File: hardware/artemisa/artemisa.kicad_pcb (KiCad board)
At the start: 2 copper layers, 140 parts, among them J1 PS2_CONN, J2 MSX_Slot, J3 MSX_Slot, J4 CONN_JOY, J5 CONN_JOY, J6 PWR_conn, J7 Audio_conn, J8 Audio_conn, J9 GFX_Connector_Output, U1 74HC32, U11 74HCT244, U12 74HCT244, U13 74HCT245, U14 74HCT244, U15 74HC74, U16 74HC08, U17 74HC32, U18 Z84C00, U19 82C55A, U2 74HC04, U20 74HC153, U21 74HC139, U22 LM311, U23 74HC138, U24 74HC32, U25 SST39SF0x0, U26 ATMEGA328P, U27 74HC154, U28 74HC595, U29 74HC595, U3 HM62256ALP-10, U30 74HC595, U31 74HC595, U32 74HC595, U33 74HC595, U34 74HC595, U35 74HC595, U36 74HC595, U37 74HC595, U38 4069, U39 74HC07, U4 HM62256ALP-10, U40 74HC74, U41 AY-3-8910, U42 74HC157, U43 74HC157, U44 74HC595, U5 74HCT11, Y1 3.58Mhz, Y2 16Mhz

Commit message: Complete layout of footprints for 25x15cm
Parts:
- added G***: LOGO, artemisa:MSX_logo, F.Cu at (62.9, 92.7)
- moved U25 135.6 mm to (228.6, 124.5)
- moved DC25 129.9 mm to (237.5, 120.7)
- moved DC26 117.7 mm to (288.9, 207.6), turned to 270 degrees
- moved C3 105.5 mm to (284.5, 201.3), turned to 0 degrees
- moved R19 104.8 mm to (132.7, 190.5)
- moved U26 104.6 mm to (292.7, 192.4)
- moved Y2 102.1 mm to (280.0, 208.8)
- moved C4 102.0 mm to (284.5, 215.3), turned to 0 degrees
- moved U1 99.6 mm to (229.2, 179.7), turned to 90 degrees
- moved U33 93.5 mm to (282.6, 188.0), turned to 90 degrees
- moved U44 92.6 mm to (282.6, 124.5), turned to 90 degrees
- moved U17 92.1 mm to (77.5, 153.0)
- moved DC17 92.1 mm to (82.5, 149.2)
- moved DC1 90.7 mm to (225.4, 174.7), turned to 270 degrees
- moved DC44 90.2 mm to (278.8, 119.4), turned to 270 degrees
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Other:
- board text added: "Artemisa MSX Computer System Motherboard Rev01 Copyright (c) 2018 Alvaro Polo"

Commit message: Add decoupling capacitors for power input
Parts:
- added C14: 10uF, artemisa:Radial_capacitor, F.Cu at (74.3, 104.2)
- added C15: 100uF, artemisa:Radial_capacitor, F.Cu at (85.7, 104.2)

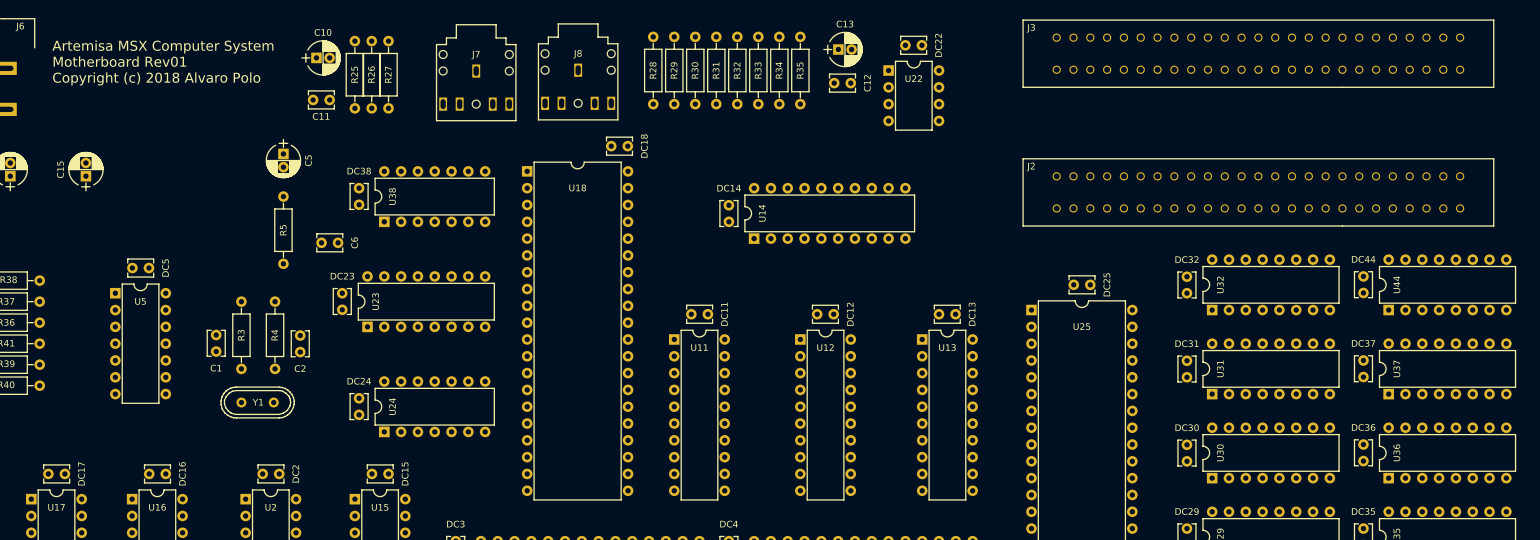
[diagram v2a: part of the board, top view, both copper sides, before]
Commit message: Make room for cartridge slots
We need more space according to cartridge specs.
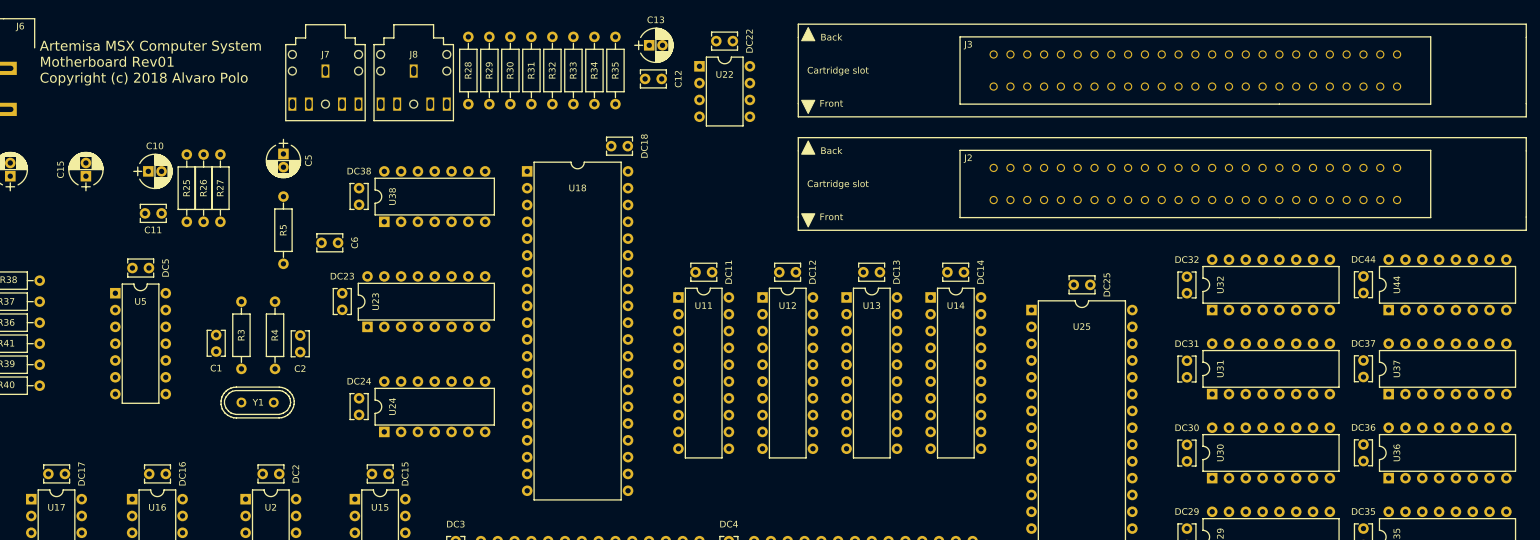
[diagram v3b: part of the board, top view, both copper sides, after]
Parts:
- moved DC14 36.9 mm to (218.4, 118.7), turned to 180 degrees
- moved C11 30.6 mm to (97.2, 109.9)
- moved R26 30.6 mm to (103.5, 101.0)
- moved C10 30.6 mm to (95.2, 103.5)
- moved R25 30.6 mm to (101.0, 111.1)
- moved R27 30.6 mm to (106.0, 111.1)
- moved DC22 28.6 mm to (183.5, 83.8)
- moved C12 28.6 mm to (172.7, 89.5)
- moved C13 28.6 mm to (170.8, 84.5)
- moved U22 28.6 mm to (178.4, 87.6)
- moved U14 28.1 mm to (213.4, 122.6), turned to 0 degrees
- moved R28 27.9 mm to (143.5, 93.3)
- moved R29 27.9 mm to (146.7, 93.3)
- moved R30 27.9 mm to (149.9, 83.2)
- moved R31 27.9 mm to (153.0, 93.3)
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
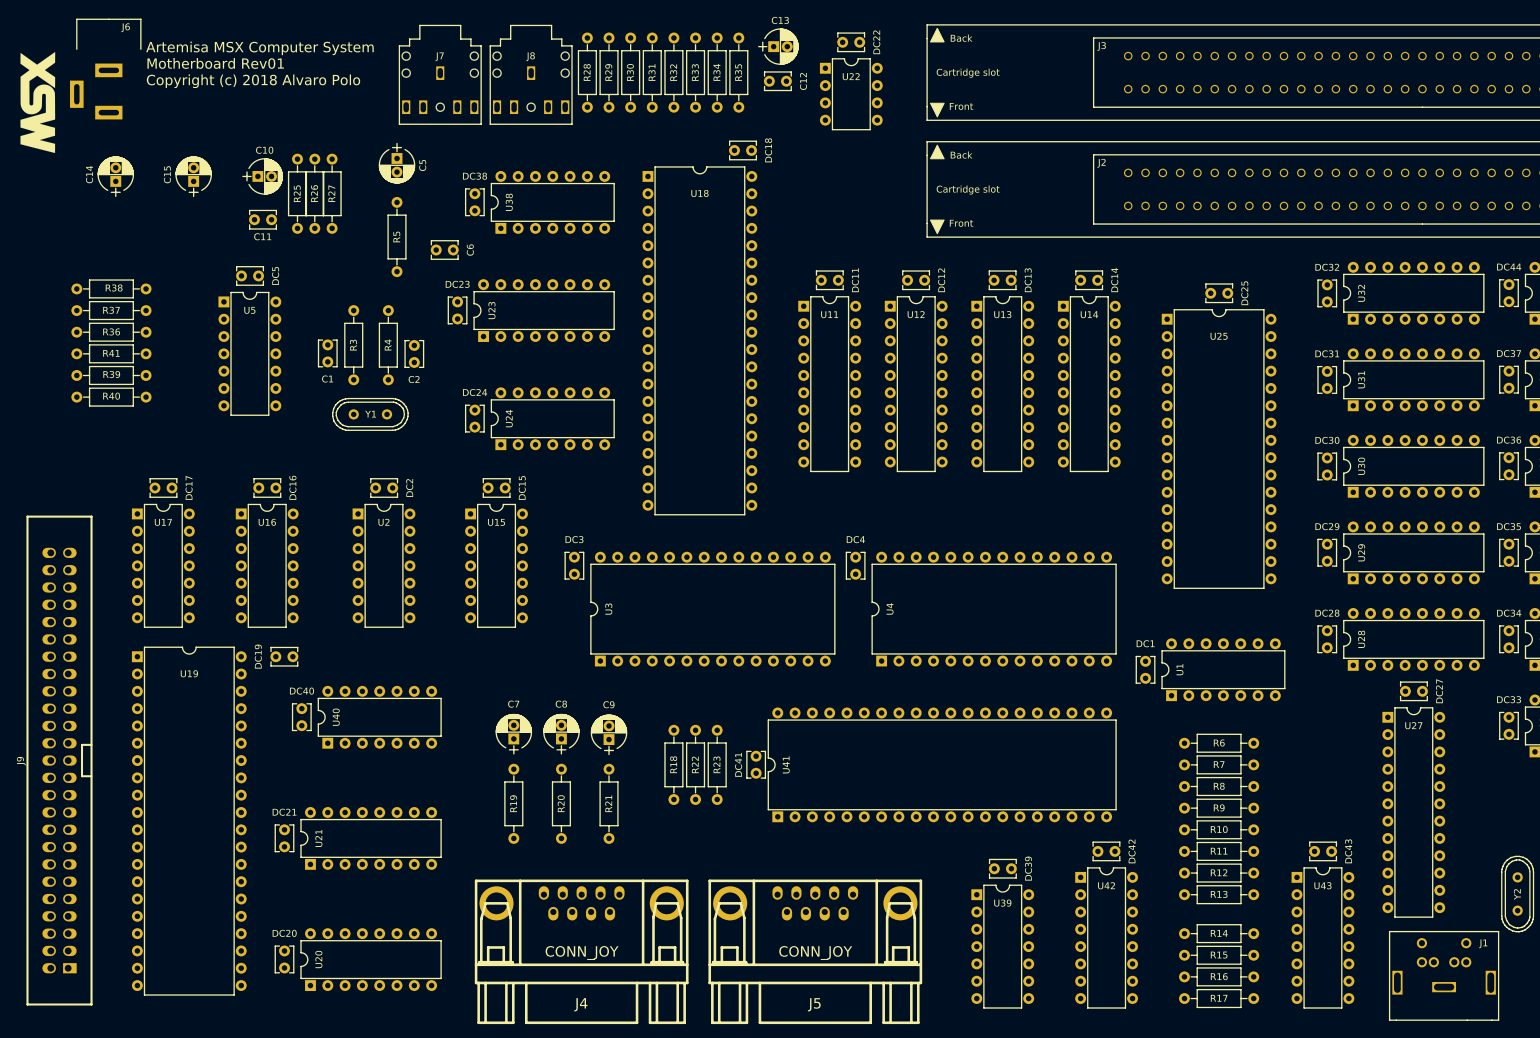
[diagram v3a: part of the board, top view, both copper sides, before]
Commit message: Move PPI close to the keyboard matrix
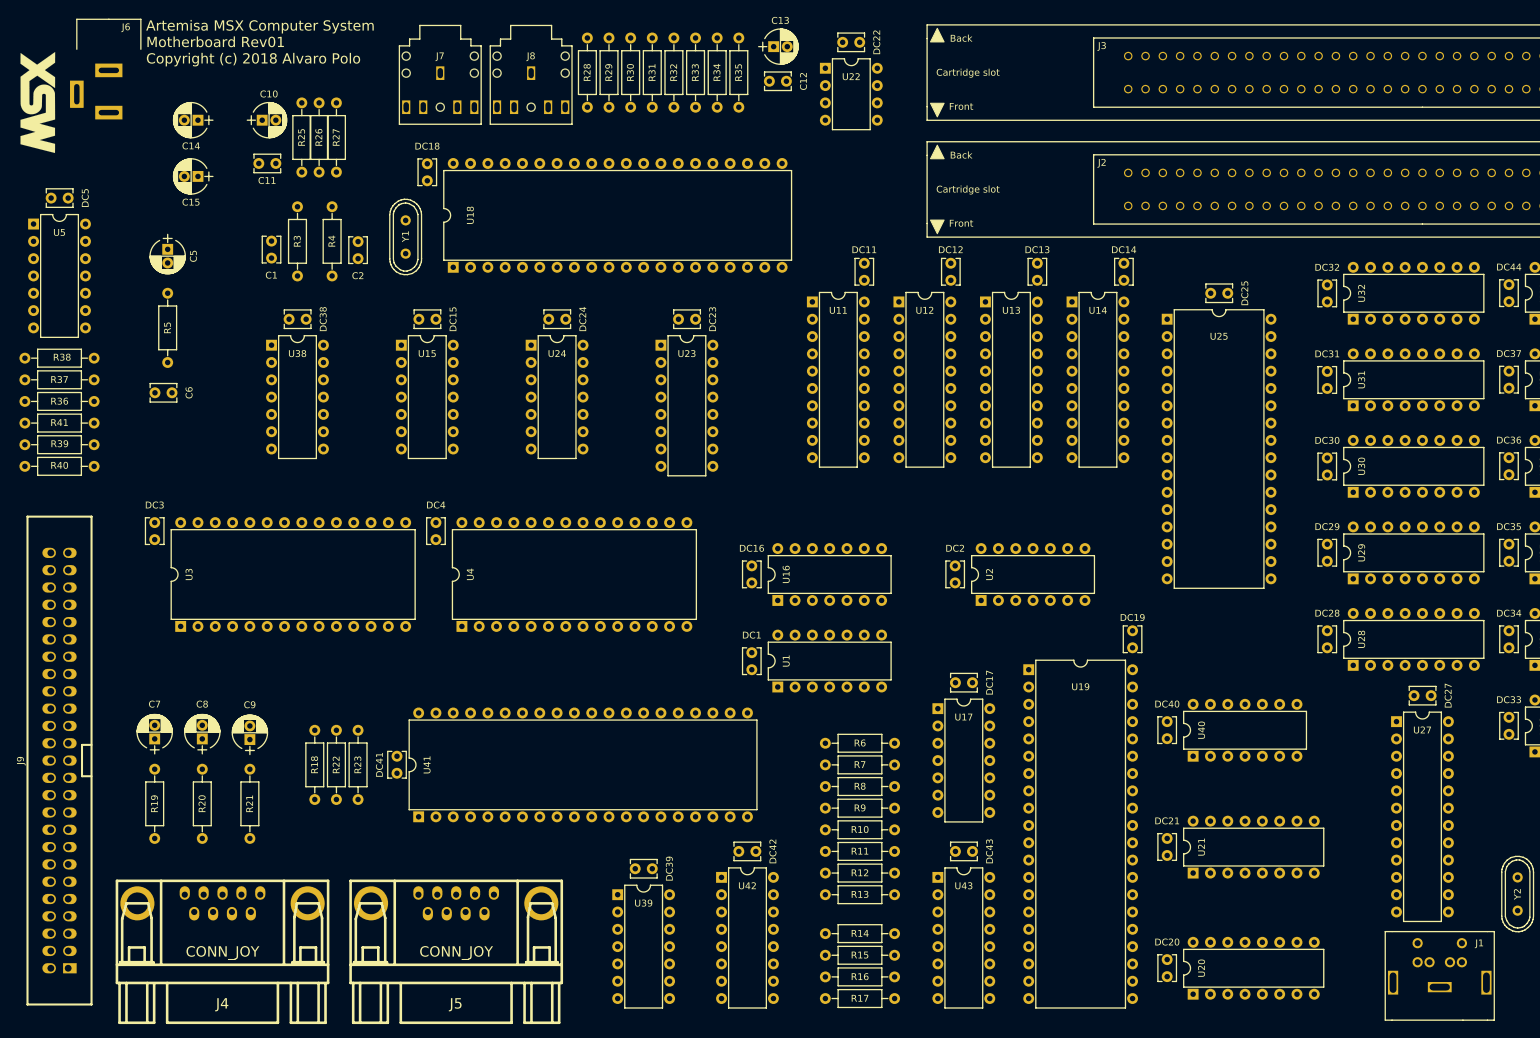
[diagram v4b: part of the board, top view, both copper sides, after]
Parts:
- moved U19 130.8 mm to (208.3, 175.9)
- moved DC20 129.5 mm to (228.6, 218.4)
- moved DC21 129.5 mm to (228.6, 200.7)
- moved U20 129.5 mm to (232.4, 223.5)
- moved U21 129.5 mm to (232.4, 205.7)
- moved DC40 127.0 mm to (228.6, 183.5)
- moved U40 127.0 mm to (232.4, 188.6)
- moved DC19 125.7 mm to (223.5, 172.7), turned to 90 degrees
- moved DC17 120.9 mm to (200.0, 177.8)
- moved U17 120.9 mm to (194.9, 181.6)
- moved U2 92.3 mm to (201.3, 165.7), turned to 90 degrees
- moved DC2 83.3 mm to (197.5, 160.7), turned to 270 degrees
- moved U16 79.8 mm to (171.4, 165.7), turned to 90 degrees
- moved DC16 70.8 mm to (167.6, 160.7), turned to 270 degrees
- moved DC4 61.8 mm to (121.3, 154.3)
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
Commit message: Align GFX connectors
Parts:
- moved DC5 8.47 mm to (75.6, 104.8), turned to 270 degrees
- moved J9 6.35 mm to (66.0, 182.9)
- moved U5 6.25 mm to (64.8, 104.8)
- moved R36 5.68 mm to (73.7, 131.4)
- moved R38 5.68 mm to (73.7, 125.1)
- moved R39 5.68 mm to (73.7, 137.8)
- moved R40 5.68 mm to (73.7, 141.0)
- moved R37 5.68 mm to (73.7, 128.3)
- moved R41 5.68 mm to (73.7, 134.6)
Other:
- board text added: "Graphics card connector"
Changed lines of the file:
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@@
   (general
     (thickness 1.6)
-    (drawings 8)
+    (drawings 9)
     (tracks 0)
     (zones 0)
@@
   )
   (module artemisa:DIP-14_300 (layer F.Cu)
-    (at 62.23 110.49)
+    (at 64.77 104.775)
     (descr "14-lead dip package, row spacing 7.62 mm (300 mils)")
     (tags "DIL DIP PDIP 2.54mm 7.62mm 300mil")
@@
   )
   (module artemisa:Disc_capacitor (layer F.Cu)
-    (at 67.31 106.68 180)
+    (at 75.565 104.775 270)
     (descr "C, Disc series, Radial, pin pitch=2.50mm, , diameter*width=3.8*2.6mm^2, Capacitor, http://www.vishay.com/docs/45233/krseries.pdf")
     (tags "C Disc series Radial pin pitch 2.50mm  diameter 3.8mm width 2.6mm Capacitor")
-    (fp_text reference DC5 (at -2.54 0 -90) (layer F.SilkS)
+    (fp_text reference DC5 (at -2.54 0) (layer F.SilkS)
       (effects (font (size 1 1) (thickness 0.15)))
     )
-    (fp_text value 100nF (at 5.08 0 -90) (layer F.Fab)
+    (fp_text value 100nF (at 5.08 0) (layer F.Fab)
       (effects (font (size 1 1) (thickness 0.15)))
     )
-    (fp_text user %R (at -2.54 0 -90) (layer F.Fab)
+    (fp_text user %R (at -2.54 0) (layer F.Fab)
       (effects (font (size 1 1) (thickness 0.15)))
     )
@@
     (fp_line (start -0.65 1.3) (end 3.15 1.3) (layer F.Fab) (width 0.1))
     (fp_line (start -0.65 -1.3) (end -0.65 1.3) (layer F.Fab) (width 0.1))
-    (pad 2 thru_hole circle (at 2.5 0 180) (size 1.6 1.6) (drill 0.8) (layers *.Cu *.Mask)
+    (pad 2 thru_hole circle (at 2.5 0 270) (size 1.6 1.6) (drill 0.8) (layers *.Cu *.Mask)
       (net 1 GND))
-    (pad 1 thru_hole circle (at 0 0 180) (size 1.6 1.6) (drill 0.8) (layers *.Cu *.Mask)
+    (pad 1 thru_hole circle (at 0 0 270) (size 1.6 1.6) (drill 0.8) (layers *.Cu *.Mask)
       (net 13 VCC))
     (model ${KIPRJMOD}/../libs/artemisa.3dshapes/Disc_capacitor.wrl
@@
   )
   (module artemisa:GFX_conn (layer F.Cu)
-    (at 66.04 189.23 90)
+    (at 66.04 182.88 90)
     (descr "Box header 25x2pin 2.54mm")
     (tags "CONN DEV")
-    (fp_text reference J9 (at 0 -5.7 90) (layer F.SilkS)
+    (fp_text reference J9 (at -34.29 -2.54 90) (layer F.SilkS)
       (effects (font (size 1 1) (thickness 0.2032)))
     )
@@
   )
   (module artemisa:Axial_resistor (layer F.Cu)
-    (at 71.12 136.525 180)
+    (at 73.66 131.445 180)
     (descr "Resistor, Axial_DIN0207 series, Axial, Horizontal, pin pitch=10.16mm, 0.25W = 1/4W, length*diameter=6.3*2.5mm^2, http://cdn-reichelt.de/documents/datenblatt/B400/1_4W%23YAG.pdf")
     (tags "Resistor Axial_DIN0207 series Axial Horizontal pin pitch 10.16mm 0.25W = 1/4W length 6.3mm diameter 2.5mm")
@@
   )
   (module artemisa:Axial_resistor (layer F.Cu)
-    (at 71.12 133.35 180)
+    (at 73.66 128.27 180)
     (descr "Resistor, Axial_DIN0207 series, Axial, Horizontal, pin pitch=10.16mm, 0.25W = 1/4W, length*diameter=6.3*2.5mm^2, http://cdn-reichelt.de/documents/datenblatt/B400/1_4W%23YAG.pdf")
     (tags "Resistor Axial_DIN0207 series Axial Horizontal pin pitch 10.16mm 0.25W = 1/4W length 6.3mm diameter 2.5mm")
@@
   )
   (module artemisa:Axial_resistor (layer F.Cu)
-    (at 71.12 130.175 180)
+    (at 73.66 125.095 180)
     (descr "Resistor, Axial_DIN0207 series, Axial, Horizontal, pin pitch=10.16mm, 0.25W = 1/4W, length*diameter=6.3*2.5mm^2, http://cdn-reichelt.de/documents/datenblatt/B400/1_4W%23YAG.pdf")
     (tags "Resistor Axial_DIN0207 series Axial Horizontal pin pitch 10.16mm 0.25W = 1/4W length 6.3mm diameter 2.5mm")
@@
   )
   (module artemisa:Axial_resistor (layer F.Cu)
-    (at 71.12 142.875 180)
+    (at 73.66 137.795 180)
     (descr "Resistor, Axial_DIN0207 series, Axial, Horizontal, pin pitch=10.16mm, 0.25W = 1/4W, length*diameter=6.3*2.5mm^2, http://cdn-reichelt.de/documents/datenblatt/B400/1_4W%23YAG.pdf")
     (tags "Resistor Axial_DIN0207 series Axial Horizontal pin pitch 10.16mm 0.25W = 1/4W length 6.3mm diameter 2.5mm")
@@
   )
   (module artemisa:Axial_resistor (layer F.Cu)
-    (at 71.12 146.05 180)
+    (at 73.66 140.97 180)
     (descr "Resistor, Axial_DIN0207 series, Axial, Horizontal, pin pitch=10.16mm, 0.25W = 1/4W, length*diameter=6.3*2.5mm^2, http://cdn-reichelt.de/documents/datenblatt/B400/1_4W%23YAG.pdf")
     (tags "Resistor Axial_DIN0207 series Axial Horizontal pin pitch 10.16mm 0.25W = 1/4W length 6.3mm diameter 2.5mm")
@@
   )
   (module artemisa:Axial_resistor (layer F.Cu)
-    (at 71.12 139.7 180)
+    (at 73.66 134.62 180)
     (descr "Resistor, Axial_DIN0207 series, Axial, Horizontal, pin pitch=10.16mm, 0.25W = 1/4W, length*diameter=6.3*2.5mm^2, http://cdn-reichelt.de/documents/datenblatt/B400/1_4W%23YAG.pdf")
     (tags "Resistor Axial_DIN0207 series Axial Horizontal pin pitch 10.16mm 0.25W = 1/4W length 6.3mm diameter 2.5mm")
@@
     )
   )
+  (gr_text "Graphics card connector" (at 72.39 147.32 90) (layer F.SilkS)
+    (effects (font (size 1 1) (thickness 0.15)) (justify right))
+  )
   (gr_text "Artemisa MSX Computer System\nMotherboard Rev01\nCopyright (c) 2018 Alvaro Polo" (at 78.74 83.82) (layer F.SilkS)

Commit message: Add mounting holes to the PCB
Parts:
- added REF**: MountingHole_M3, artemisa:Mounting_hole_M3, F.Cu at (182.9, 224.8)
- added REF**: MountingHole_M3, artemisa:Mounting_hole_M3, F.Cu at (182.9, 82.5)
- added REF**: MountingHole_M3, artemisa:Mounting_hole_M3, F.Cu at (302.9, 82.5)
- added REF**: MountingHole_M3, artemisa:Mounting_hole_M3, F.Cu at (302.9, 224.8)
- added REF**: MountingHole_M3, artemisa:Mounting_hole_M3, F.Cu at (61.0, 224.8)
- added REF**: MountingHole_M3, artemisa:Mounting_hole_M3, F.Cu at (61.0, 82.5)
- moved DC22 5.08 mm to (183.5, 88.9)
- moved R15 5.08 mm to (188.6, 212.7)
- moved R17 5.08 mm to (188.6, 219.1)
- moved U22 5.08 mm to (178.4, 92.7)
- moved R14 5.08 mm to (188.6, 209.6)
- moved R16 5.08 mm to (188.6, 215.9)
- moved C4 4.62 mm to (280.0, 216.5), turned to 270 degrees
- moved C3 4.49 mm to (280.0, 200.7), turned to 90 degrees
- moved U26 4.44 mm to (288.3, 192.4)
- moved DC26 3.81 mm to (285.1, 207.6)
- moved R11 3.81 mm to (178.4, 198.8)
- moved R12 3.81 mm to (178.4, 201.9)
- moved R13 3.81 mm to (178.4, 205.1)
- moved R6 3.81 mm to (178.4, 182.9)
- moved R7 3.81 mm to (178.4, 186.1)
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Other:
- board text added: "Artemisa MSX Computer System Motherboard Mk I - Rev01 Copyright (c) 2018 Alvaro Polo"
- board text removed: "Artemisa MSX Computer System Motherboard Rev01 Copyright (c) 2018 Alvaro Polo"

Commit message: Trace the whole motherboard PCB
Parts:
- moved R6 79.0 mm to (101.6, 201.3)
- moved R7 79.0 mm to (101.6, 204.5)
- moved U2 65.2 mm to (148.0, 128.3), turned to 0 degrees
- moved R8 64.6 mm to (114.9, 201.3)
- moved R9 64.6 mm to (114.9, 204.5)
- moved U1 62.6 mm to (134.0, 128.3), turned to 0 degrees
- moved DC2 57.3 mm to (153.0, 124.5), turned to 180 degrees
- moved DC1 56.7 mm to (139.0, 124.5), turned to 180 degrees
- moved U21 52.5 mm to (185.4, 182.2), turned to 0 degrees
- moved R10 50.5 mm to (128.3, 201.3)
- moved R11 50.5 mm to (128.3, 204.5)
- moved DC19 49.9 mm to (253.4, 212.7), turned to 270 degrees
- moved DC25 46.6 mm to (228.6, 166.4), turned to 270 degrees
- moved U25 46.4 mm to (210.2, 167.0)
- moved DC21 44.1 mm to (190.5, 178.4), turned to 180 degrees
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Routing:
- net VCC: track 0.00 -> 1738.8 mm, vias 0 -> 10
- net /~RESET: track 0.00 -> 550.4 mm, vias 0 -> 6
- net /ADDR15: track 0.00 -> 536.5 mm, vias 0 -> 12
- net /ADDR4: track 0.00 -> 501.0 mm, vias 0 -> 9
- net /ADDR14: track 0.00 -> 494.4 mm, vias 0 -> 12
- net /CPU/DATA4: track 0.00 -> 488.4 mm, vias 0 -> 10
- net /CPU/DATA3: track 0.00 -> 487.3 mm, vias 0 -> 12
- net /CPU/DATA6: track 0.00 -> 478.2 mm, vias 0 -> 11
- net /CPU/DATA7: track 0.00 -> 470.4 mm, vias 0 -> 11
- net /CPU/DATA5: track 0.00 -> 468.8 mm, vias 0 -> 9
- net /CPU/DATA0: track 0.00 -> 454.9 mm, vias 0 -> 11
- net /CPU/DATA2: track 0.00 -> 451.3 mm, vias 0 -> 11
- net /~RD: track 0.00 -> 444.6 mm, vias 0 -> 9
- net /CPU/DATA1: track 0.00 -> 443.0 mm, vias 0 -> 11
- net /ADDR1: track 0.00 -> 428.2 mm, vias 0 -> 10
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- added copper zone on B.Cu, net GND
- added copper zone on F.Cu, net GND

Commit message: Add power LED to the PCB
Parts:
- added D1: PWR LED, artemisa:LED, F.Cu at (62.9, 89.5)
- added R1: 220, artemisa:Axial_resistor, F.Cu at (61.0, 105.4)
- moved G*** 264.4 mm to (301.6, 207.6)
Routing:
- net VCC: track 1738.8 -> 1758.4 mm
- net Net-(D1-Pad1): track 0.00 -> 5.23 mm
- net Net-(J7-Pad2): track 13.6 -> 13.0 mm
